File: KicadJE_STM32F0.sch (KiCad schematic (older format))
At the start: 101 parts, among them J401 CV1, J402 CV2, J403 OUT1, J404 OUT2, J405 OUT3, J406 OUT4, J407 IN1, J408 IN2, J409 I2C, P401 Doepfer_Power_16pin, SW401 SW_SPDT, U401 TL072, U402 TL072, U405 MCP4822

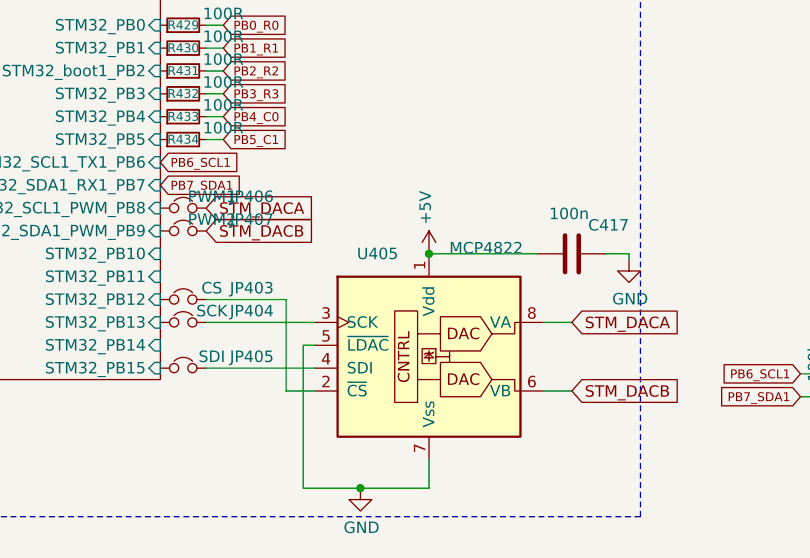
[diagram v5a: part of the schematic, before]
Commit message: MCP to GNDA and 3.3VA
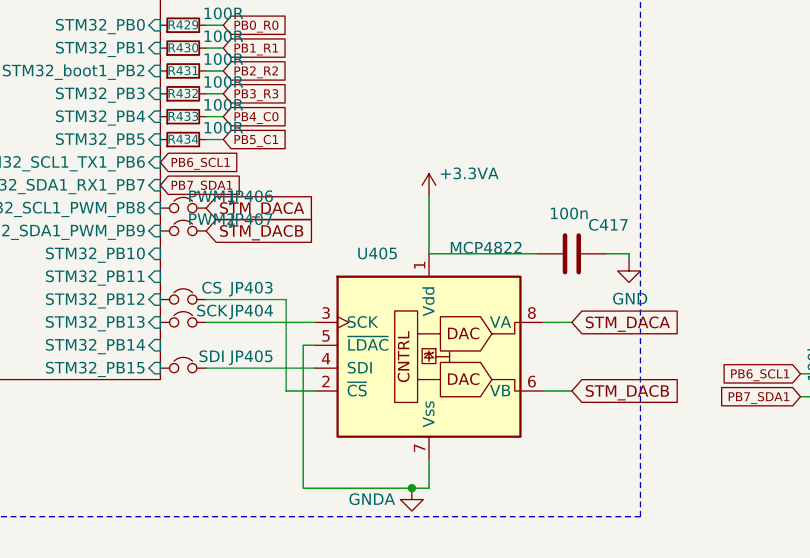
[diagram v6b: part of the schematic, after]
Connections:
- net +5V: no longer C417.1, U405.1 (Vdd)
- net GND: no longer U405.5 (~LDAC), U405.7 (Vss)
- net GNDA: now also U405.5 (~LDAC), U405.7 (Vss)
- new net +3.3VA: C417.1, U405.1 (Vdd)
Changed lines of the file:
@@
 $EndSheet
 Wire Wire Line
-	4425 7625 4125 7625
-$Comp
-L Envelope-cache-2018-08-04-13-00-04:GND #PWR?
-U 1 1 5CFF8C91
-P 4125 7625
-AR Path="/5CFF8C91" Ref="#PWR?"  Part="1"
-AR Path="/5CD3F059/5CFF8C91" Ref="#PWR?"  Part="1"
-AR Path="/5CE53731/5CFF8C91" Ref="#PWR0440"  Part="1"
-F 0 "#PWR0440" H 4125 7375 50  0001 C CNN
-F 1 "GND" H 4130 7452 50  0000 C CNN
-F 2 "" H 4125 7625 50  0001 C CNN
-F 3 "" H 4125 7625 50  0001 C CNN
-	1    4125 7625
-	1    0    0    -1
-$EndComp
-Connection ~ 4125 7625
-Wire Wire Line
-	4125 7625 3875 7625
+	4425 7625 4350 7625
 Wire Wire Line
 	3925 6900 3450 6900
@@
 STM_DACA
 $Comp
-L Envelope-cache-2018-08-04-13-00-04:+5V #PWR?
-U 1 1 5D1CE224
-P 4425 6600
-AR Path="/5D1CE224" Ref="#PWR?"  Part="1"
-AR Path="/5CE53731/5D1CE224" Ref="#PWR0436"  Part="1"
-F 0 "#PWR0436" H 4425 6450 50  0001 C CNN
-F 1 "+5V" V 4440 6728 50  0000 L CNN
-F 2 "" H 4425 6600 50  0001 C CNN
-F 3 "" H 4425 6600 50  0001 C CNN
-	1    4425 6600
-	-1   0    0    -1
-$EndComp
-$Comp
 L Envelope-cache-2018-08-04-13-00-04:GND #PWR?
 U 1 1 5D1D0E13
@@
 Wire Wire Line
 	4900 6600 4425 6600
-Connection ~ 4425 6600
 $Comp
 L Device:D D?
@@
 	3300 825  3425 825
 Connection ~ 3300 825
+$Comp
+L power:GNDA #PWR?
+U 1 1 5D8A5A17
+P 4350 7625
+AR Path="/5D8A5A17" Ref="#PWR?"  Part="1"
+AR Path="/5CD3F059/5D8A5A17" Ref="#PWR?"  Part="1"
+AR Path="/5CE53731/5D8A5A17" Ref="#PWR?"  Part="1"
+F 0 "#PWR?" H 4350 7375 50  0001 C CNN
+F 1 "GNDA" H 4525 7575 50  0000 C CNN
+F 2 "" H 4350 7625 50  0001 C CNN
+F 3 "" H 4350 7625 50  0001 C CNN
+	1    4350 7625
+	-1   0    0    -1
+$EndComp
+Connection ~ 4350 7625
+Wire Wire Line
+	3875 7625 4350 7625
+$Comp
+L power:+3.3VA #PWR?
+U 1 1 5D8A8F3A
+P 4425 6350
+F 0 "#PWR?" H 4425 6200 50  0001 C CNN
+F 1 "+3.3VA" H 4600 6450 50  0000 C CNN
+F 2 "" H 4425 6350 50  0001 C CNN
+F 3 "" H 4425 6350 50  0001 C CNN
+	1    4425 6350
+	1    0    0    -1
+$EndComp
+Wire Wire Line
+	4425 6350 4425 6600
 $EndSCHEMATC

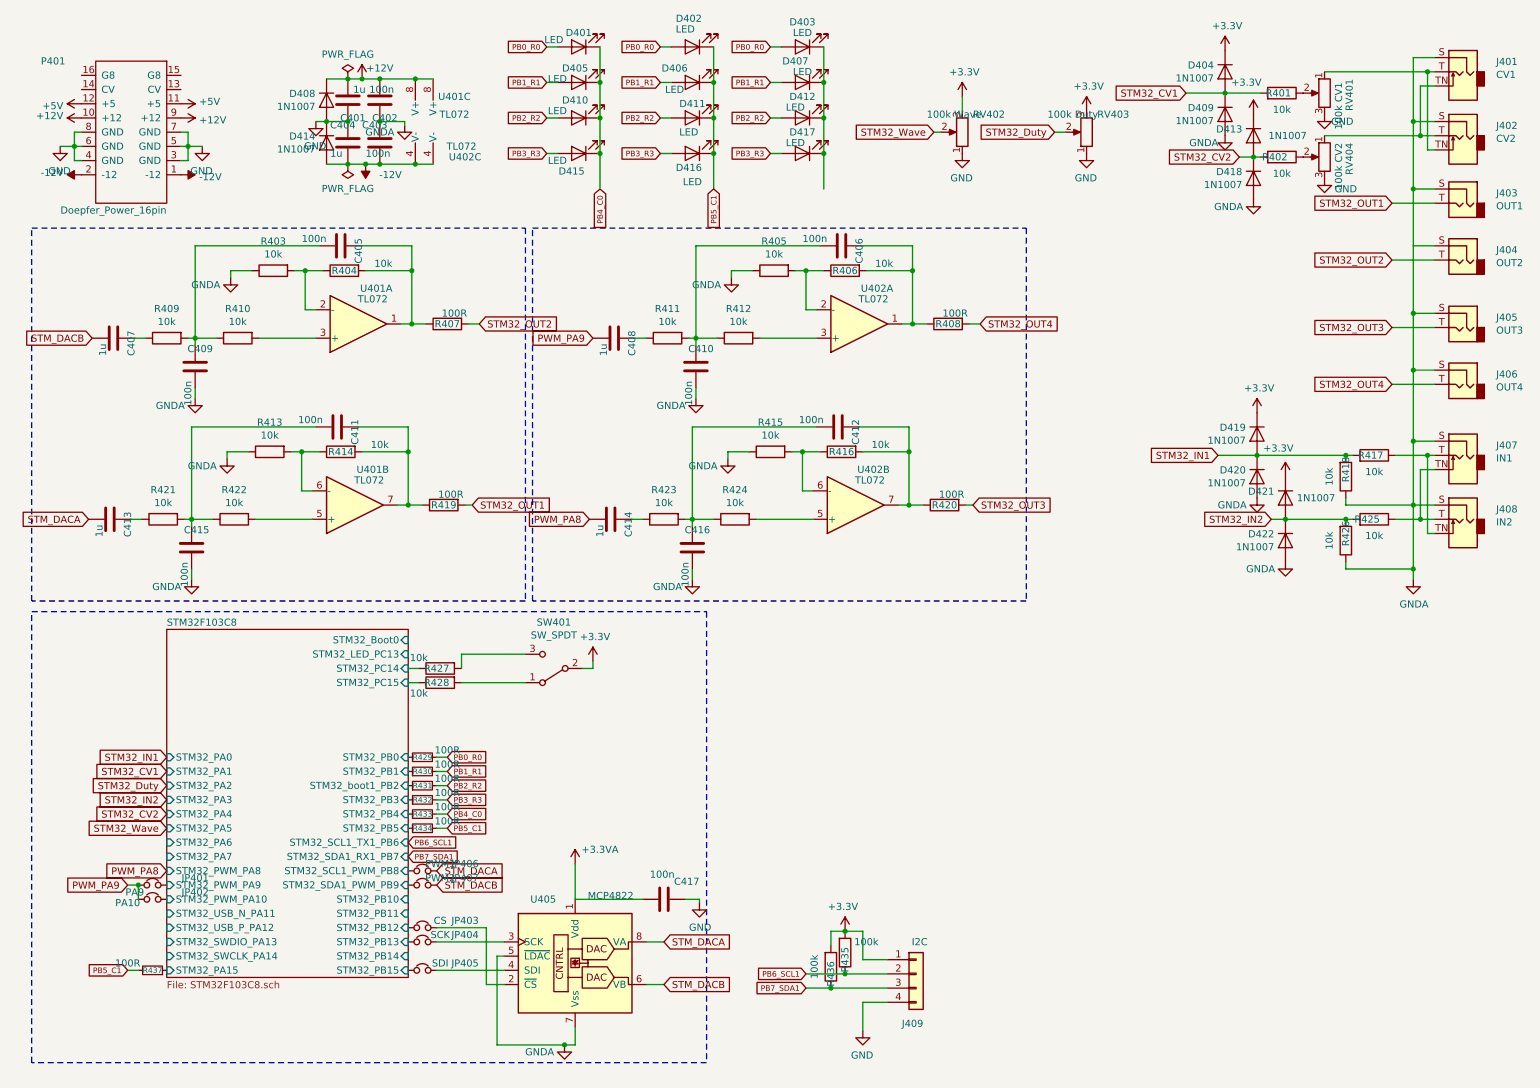
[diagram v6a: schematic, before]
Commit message: Missing Column Driver for column 2 - STM32
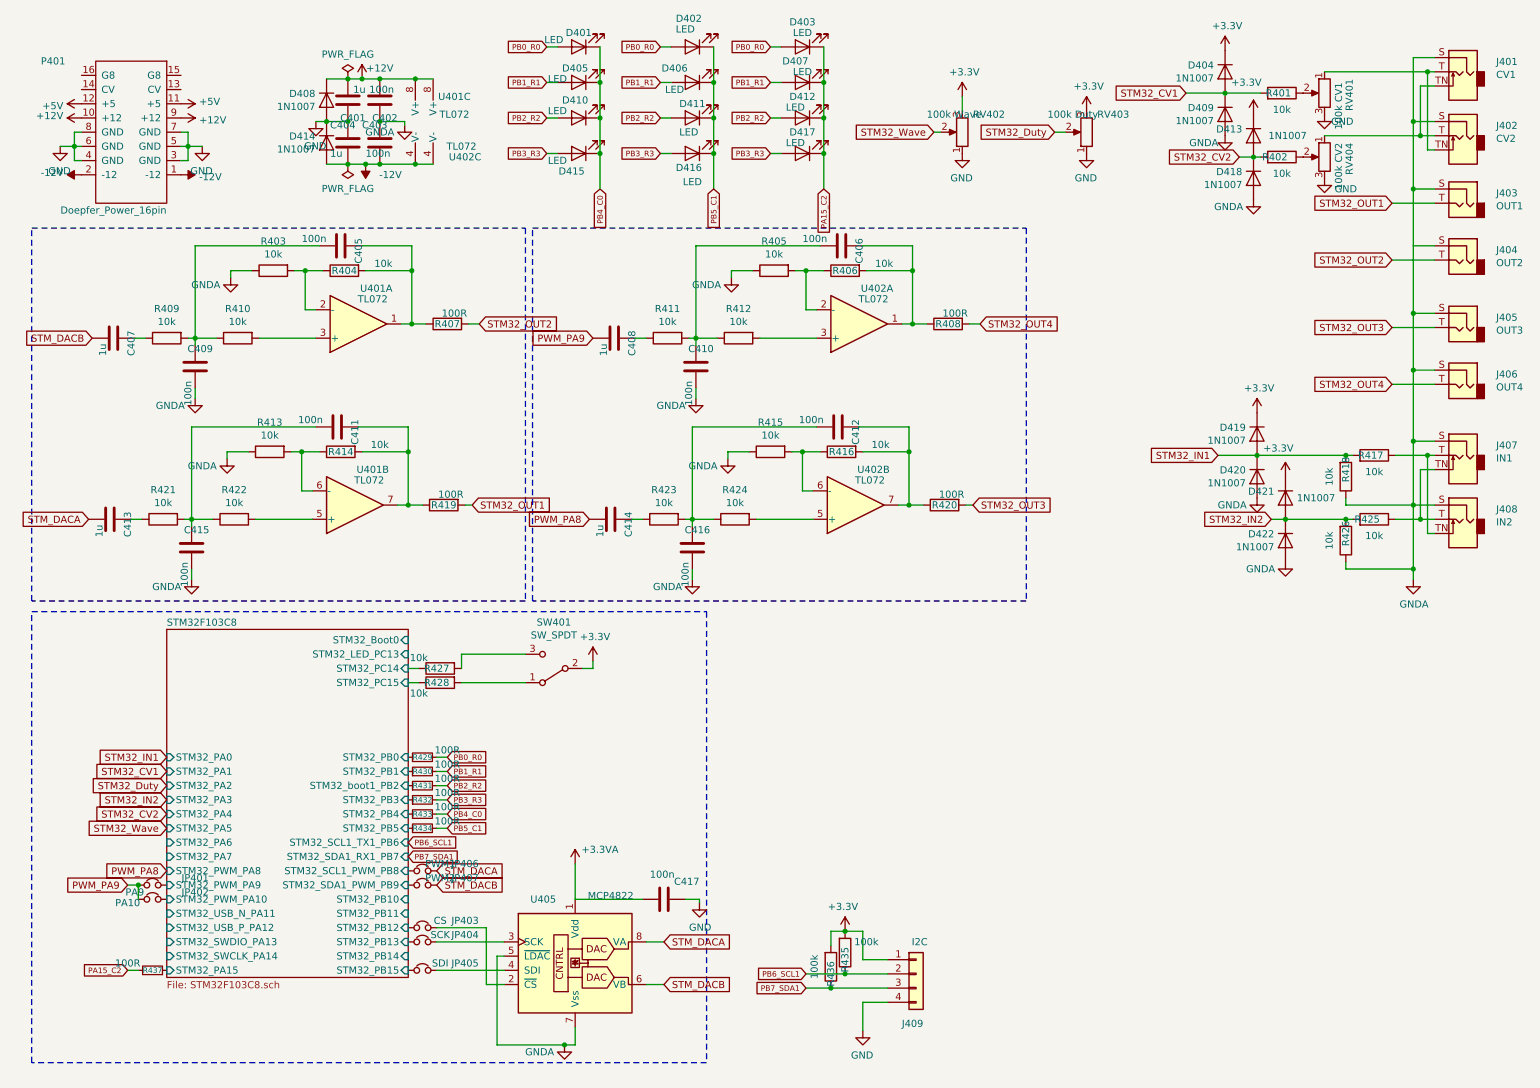
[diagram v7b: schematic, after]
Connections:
- net PB5_C1: no longer R437.2
- net PA15_C2: now reaches D403.1 (K), D407.1 (K), D412.1 (K), D417.1 (K)
- net PA15_C2: now also R437.2
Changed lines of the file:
@@
 PB3_R3
 Text GLabel 1275 7100 0    39   Input ~ 0
-PB5_C1
+PA15_C2
 Wire Wire Line
 	1275 7100 1350 7100
@@
 AR Path="/5D8A5A17" Ref="#PWR?"  Part="1"
 AR Path="/5CD3F059/5D8A5A17" Ref="#PWR?"  Part="1"
-AR Path="/5CE53731/5D8A5A17" Ref="#PWR?"  Part="1"
-F 0 "#PWR?" H 4350 7375 50  0001 C CNN
+AR Path="/5CE53731/5D8A5A17" Ref="#PWR0104"  Part="1"
+F 0 "#PWR0104" H 4350 7375 50  0001 C CNN
 F 1 "GNDA" H 4525 7575 50  0000 C CNN
 F 2 "" H 4350 7625 50  0001 C CNN
@@
 U 1 1 5D8A8F3A
 P 4425 6350
-F 0 "#PWR?" H 4425 6200 50  0001 C CNN
+AR Path="/5CE53731/5CEC50C7/5D8A8F3A" Ref="#PWR?"  Part="1"
+AR Path="/5CE53731/5D8A8F3A" Ref="#PWR0105"  Part="1"
+F 0 "#PWR0105" H 4425 6200 50  0001 C CNN
 F 1 "+3.3VA" H 4600 6450 50  0000 C CNN
 F 2 "" H 4425 6350 50  0001 C CNN
@@
 Wire Wire Line
 	4425 6350 4425 6600
+Text GLabel 6175 1600 3    39   Input ~ 0
+PA15_C2
 $EndSCHEMATC

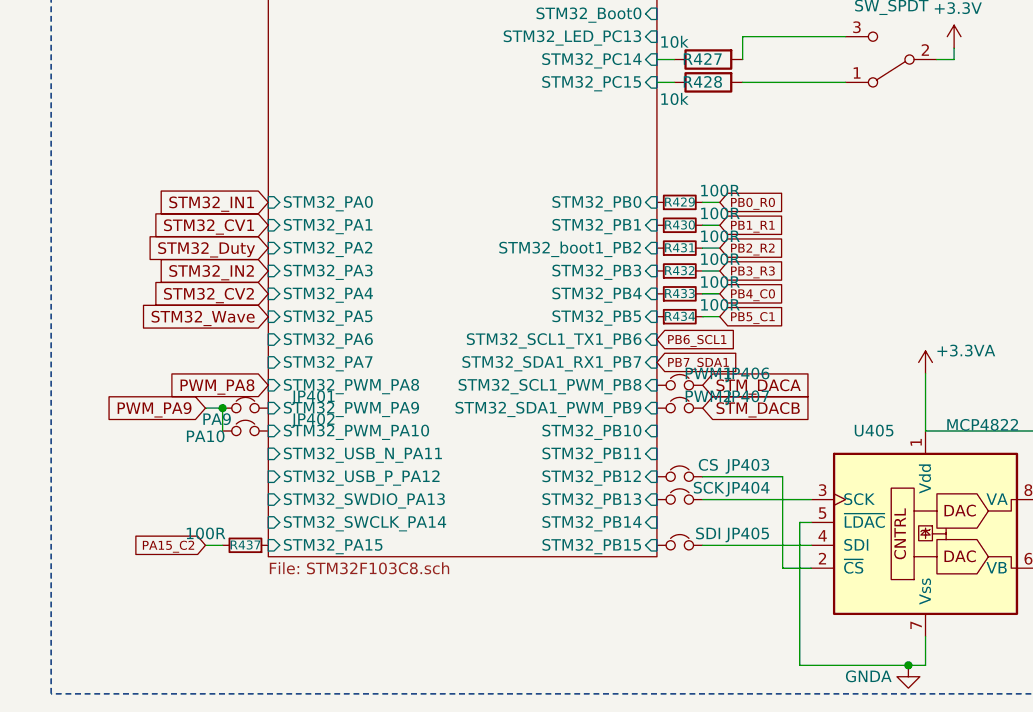
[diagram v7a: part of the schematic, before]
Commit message: tweaking vias and routing around STM32
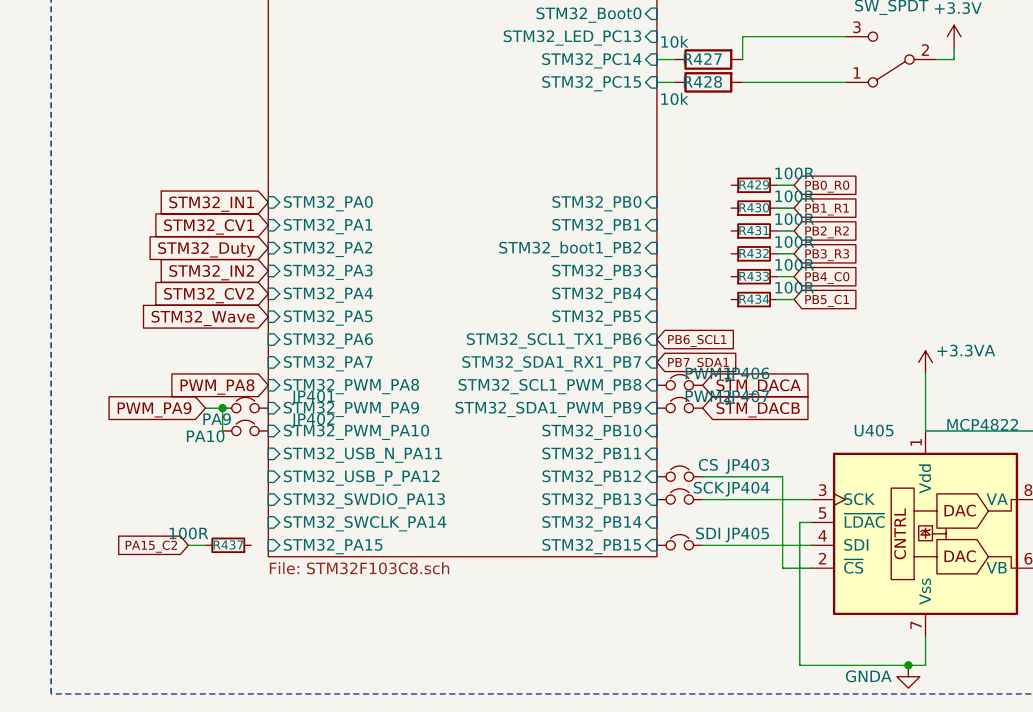
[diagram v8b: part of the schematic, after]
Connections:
- net STM32F103C8/STM32_PA15: no longer R437.1
- net STM32F103C8/STM32_PB0: no longer R429.1
- net STM32F103C8/STM32_PB1: no longer R430.1
- net STM32F103C8/STM32_PB3: no longer R432.1
- net STM32F103C8/STM32_PB4: no longer R433.1
- net STM32F103C8/STM32_PB5: no longer R434.1
- net STM32F103C8/STM32_boot1_PB2: no longer R431.1
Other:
- moved on the sheet: R429, R430, R431, R432, R433, R434, R437
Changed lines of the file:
@@
 	0    1    -1   0
 $EndComp
-Text GLabel 3525 5600 2    39   Input ~ 0
+Text GLabel 3850 5525 2    39   Input ~ 0
 PB0_R0
-Text GLabel 3525 5800 2    39   Input ~ 0
+Text GLabel 3850 5725 2    39   Input ~ 0
 PB2_R2
-Text GLabel 3525 6000 2    39   Input ~ 0
+Text GLabel 3850 5925 2    39   Input ~ 0
 PB4_C0
-Text GLabel 3525 6100 2    39   Input ~ 0
+Text GLabel 3850 6025 2    39   Input ~ 0
 PB5_C1
 Wire Wire Line
-	3525 5700 3450 5700
+	3850 5625 3775 5625
 Wire Wire Line
-	3525 5900 3450 5900
+	3850 5825 3775 5825
 Wire Wire Line
-	3525 6100 3450 6100
+	3850 6025 3775 6025
 $Comp
 L Device:R_Small R?
 U 1 1 5D0151BE
-P 3350 5600
+P 3675 5525
 AR Path="/5D0151BE" Ref="R?"  Part="1"
 AR Path="/5CD3F059/5D0151BE" Ref="R?"  Part="1"
 AR Path="/5CE3E7A9/5D0151BE" Ref="R?"  Part="1"
 AR Path="/5CE53731/5D0151BE" Ref="R429"  Part="1"
-F 0 "R429" V 3350 5600 39  0000 C CNN
-F 1 "100R" V 3400 5425 50  0000 C CNN
-F 2 "Resistor_SMD:R_0805_2012Metric_Pad1.15x1.40mm_HandSolder" V 3280 5600 50  0001 C CNN
-F 3 "~" H 3350 5600 50  0001 C CNN
-	1    3350 5600
+F 0 "R429" V 3675 5525 39  0000 C CNN
+F 1 "100R" V 3725 5350 50  0000 C CNN
+F 2 "Resistor_SMD:R_0805_2012Metric_Pad1.15x1.40mm_HandSolder" V 3605 5525 50  0001 C CNN
+F 3 "~" H 3675 5525 50  0001 C CNN
+	1    3675 5525
 	0    -1   -1   0
 $EndComp
 Wire Wire Line
-	3450 5600 3525 5600
+	3775 5525 3850 5525
 $Comp
 L Device:R_Small R?
 U 1 1 5D0151C5
-P 3350 5700
+P 3675 5625
 AR Path="/5D0151C5" Ref="R?"  Part="1"
 AR Path="/5CD3F059/5D0151C5" Ref="R?"  Part="1"
 AR Path="/5CE3E7A9/5D0151C5" Ref="R?"  Part="1"
 AR Path="/5CE53731/5D0151C5" Ref="R430"  Part="1"
-F 0 "R430" V 3350 5700 39  0000 C CNN
-F 1 "100R" V 3400 5525 50  0000 C CNN
-F 2 "Resistor_SMD:R_0805_2012Metric_Pad1.15x1.40mm_HandSolder" V 3280 5700 50  0001 C CNN
-F 3 "~" H 3350 5700 50  0001 C CNN
-	1    3350 5700
+F 0 "R430" V 3675 5625 39  0000 C CNN
+F 1 "100R" V 3725 5450 50  0000 C CNN
+F 2 "Resistor_SMD:R_0805_2012Metric_Pad1.15x1.40mm_HandSolder" V 3605 5625 50  0001 C CNN
+F 3 "~" H 3675 5625 50  0001 C CNN
+	1    3675 5625
 	0    -1   -1   0
 $EndComp
@@
 L Device:R_Small R?
 U 1 1 5D0151CB
-P 3350 5800
+P 3675 5725
 AR Path="/5D0151CB" Ref="R?"  Part="1"
 AR Path="/5CD3F059/5D0151CB" Ref="R?"  Part="1"
 AR Path="/5CE3E7A9/5D0151CB" Ref="R?"  Part="1"
 AR Path="/5CE53731/5D0151CB" Ref="R431"  Part="1"
-F 0 "R431" V 3350 5800 39  0000 C CNN
-F 1 "100R" V 3400 5625 50  0000 C CNN
-F 2 "Resistor_SMD:R_0805_2012Metric_Pad1.15x1.40mm_HandSolder" V 3280 5800 50  0001 C CNN
-F 3 "~" H 3350 5800 50  0001 C CNN
-	1    3350 5800
+F 0 "R431" V 3675 5725 39  0000 C CNN
+F 1 "100R" V 3725 5550 50  0000 C CNN
+F 2 "Resistor_SMD:R_0805_2012Metric_Pad1.15x1.40mm_HandSolder" V 3605 5725 50  0001 C CNN
+F 3 "~" H 3675 5725 50  0001 C CNN
+	1    3675 5725
 	0    -1   -1   0
 $EndComp
 Wire Wire Line
-	3450 5800 3525 5800
+	3775 5725 3850 5725
 $Comp
 L Device:R_Small R?
 U 1 1 5D0151D2
-P 3350 5900
+P 3675 5825
 AR Path="/5D0151D2" Ref="R?"  Part="1"
 AR Path="/5CD3F059/5D0151D2" Ref="R?"  Part="1"
 AR Path="/5CE3E7A9/5D0151D2" Ref="R?"  Part="1"
 AR Path="/5CE53731/5D0151D2" Ref="R432"  Part="1"
-F 0 "R432" V 3350 5900 39  0000 C CNN
-F 1 "100R" V 3400 5725 50  0000 C CNN
-F 2 "Resistor_SMD:R_0805_2012Metric_Pad1.15x1.40mm_HandSolder" V 3280 5900 50  0001 C CNN
-F 3 "~" H 3350 5900 50  0001 C CNN
-	1    3350 5900
+F 0 "R432" V 3675 5825 39  0000 C CNN
+F 1 "100R" V 3725 5650 50  0000 C CNN
+F 2 "Resistor_SMD:R_0805_2012Metric_Pad1.15x1.40mm_HandSolder" V 3605 5825 50  0001 C CNN
+F 3 "~" H 3675 5825 50  0001 C CNN
+	1    3675 5825
 	0    -1   -1   0
 $EndComp
@@
 L Device:R_Small R?
 U 1 1 5D0151D8
-P 3350 6000
+P 3675 5925
 AR Path="/5D0151D8" Ref="R?"  Part="1"
 AR Path="/5CD3F059/5D0151D8" Ref="R?"  Part="1"
 AR Path="/5CE3E7A9/5D0151D8" Ref="R?"  Part="1"
 AR Path="/5CE53731/5D0151D8" Ref="R433"  Part="1"
-F 0 "R433" V 3350 6000 39  0000 C CNN
-F 1 "100R" V 3400 5825 50  0000 C CNN
-F 2 "Resistor_SMD:R_0805_2012Metric_Pad1.15x1.40mm_HandSolder" V 3280 6000 50  0001 C CNN
-F 3 "~" H 3350 6000 50  0001 C CNN
-	1    3350 6000
+F 0 "R433" V 3675 5925 39  0000 C CNN
+F 1 "100R" V 3725 5750 50  0000 C CNN
+F 2 "Resistor_SMD:R_0805_2012Metric_Pad1.15x1.40mm_HandSolder" V 3605 5925 50  0001 C CNN
+F 3 "~" H 3675 5925 50  0001 C CNN
+	1    3675 5925
 	0    -1   -1   0
 $EndComp
 Wire Wire Line
-	3450 6000 3525 6000
+	3775 5925 3850 5925
 $Comp
 L Device:R_Small R?
 U 1 1 5D0151DF
-P 3350 6100
+P 3675 6025
 AR Path="/5D0151DF" Ref="R?"  Part="1"
 AR Path="/5CD3F059/5D0151DF" Ref="R?"  Part="1"
 AR Path="/5CE3E7A9/5D0151DF" Ref="R?"  Part="1"
 AR Path="/5CE53731/5D0151DF" Ref="R434"  Part="1"
-F 0 "R434" V 3350 6100 39  0000 C CNN
-F 1 "100R" V 3400 5925 50  0000 C CNN
-F 2 "Resistor_SMD:R_0805_2012Metric_Pad1.15x1.40mm_HandSolder" V 3280 6100 50  0001 C CNN
-F 3 "~" H 3350 6100 50  0001 C CNN
-	1    3350 6100
+F 0 "R434" V 3675 6025 39  0000 C CNN
+F 1 "100R" V 3725 5850 50  0000 C CNN
+F 2 "Resistor_SMD:R_0805_2012Metric_Pad1.15x1.40mm_HandSolder" V 3605 6025 50  0001 C CNN
+F 3 "~" H 3675 6025 50  0001 C CNN
+	1    3675 6025
 	0    -1   -1   0
 $EndComp
-Text GLabel 3525 5700 2    39   Input ~ 0
+Text GLabel 3850 5625 2    39   Input ~ 0
 PB1_R1
-Text GLabel 3525 5900 2    39   Input ~ 0
+Text GLabel 3850 5825 2    39   Input ~ 0
 PB3_R3
 $Comp
@@
 Text GLabel 5800 1350 0    39   Input ~ 0
 PB3_R3
-Text GLabel 1275 7100 0    39   Input ~ 0
+Text GLabel 1200 7100 0    39   Input ~ 0
 PA15_C2
 Wire Wire Line
-	1275 7100 1350 7100
+	1200 7100 1275 7100
 $Comp
 L Device:R_Small R?
 U 1 1 5D10D6AF
-P 1450 7100
+P 1375 7100
 AR Path="/5D10D6AF" Ref="R?"  Part="1"
 AR Path="/5CD3F059/5D10D6AF" Ref="R?"  Part="1"
 AR Path="/5CE3E7A9/5D10D6AF" Ref="R?"  Part="1"
 AR Path="/5CE53731/5D10D6AF" Ref="R437"  Part="1"
-F 0 "R437" V 1450 7100 39  0000 C CNN
-F 1 "100R" V 1500 6925 50  0000 C CNN
-F 2 "Resistor_SMD:R_0805_2012Metric_Pad1.15x1.40mm_HandSolder" V 1380 7100 50  0001 C CNN
-F 3 "~" H 1450 7100 50  0001 C CNN
-	1    1450 7100
+F 0 "R437" V 1375 7100 39  0000 C CNN
+F 1 "100R" V 1425 6925 50  0000 C CNN
+F 2 "Resistor_SMD:R_0805_2012Metric_Pad1.15x1.40mm_HandSolder" V 1305 7100 50  0001 C CNN
+F 3 "~" H 1375 7100 50  0001 C CNN
+	1    1375 7100
 	0    1    -1   0
 $EndComp
